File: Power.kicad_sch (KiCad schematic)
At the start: 14 parts, among them J2 S2B-PH-SM4-TB, Q1 DMP3099L, U2 AP2112K-3.3, U3 BQ21040DBV

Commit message: Added power latch circuit.
Signed-off-by: James Mendel <jrm.mendel@gmail.com>
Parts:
- added C7: 0.1u, symbol Device:C
- added D3, D4: MBR0520, Diode_SMD:D_SOD-123, symbol Diode:MBR0520
- added Q2: 2N7002, Package_TO_SOT_SMD:SOT-23, symbol Transistor_FET:2N7002
- added R10, R12, R13, R8, R9: 10k, symbol Device:R
- added SW1: CK_KMS2xxGP, Button_Switch_SMD:SW_SPST_CK_KMS2xxGP, symbol Switch:CK_KMS2xxGP
- D1: value CHARGE -> CHARGING
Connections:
- net +3.3V: now also D3.2 (A)
- net GND: now also C7.2, Q2.2 (S), R10.2, R13.1, R8.2, SW1.SH (B)
- net PWR_EN: now also Q2.3 (D), R12.2, R8.1
- net V_SW: now also SW1.1
- new net: D3.1 (K), D4.1 (K), R12.1
- new net: D4.2 (A), R9.2, SW1.2
- new net PWR_SW: C7.1, R10.1, R9.1
- new net SYS_PWROFF: Q2.1 (G), R13.2
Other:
- note added: "Off-Sheet Connections"
- note added: "Power Switch + Latch"
- note removed: "Todo: Power switching with tactile button."
- moved on the sheet: C3, C4, C5, C6, D1, D2, J2, Q1, R4, R5, R6, R7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

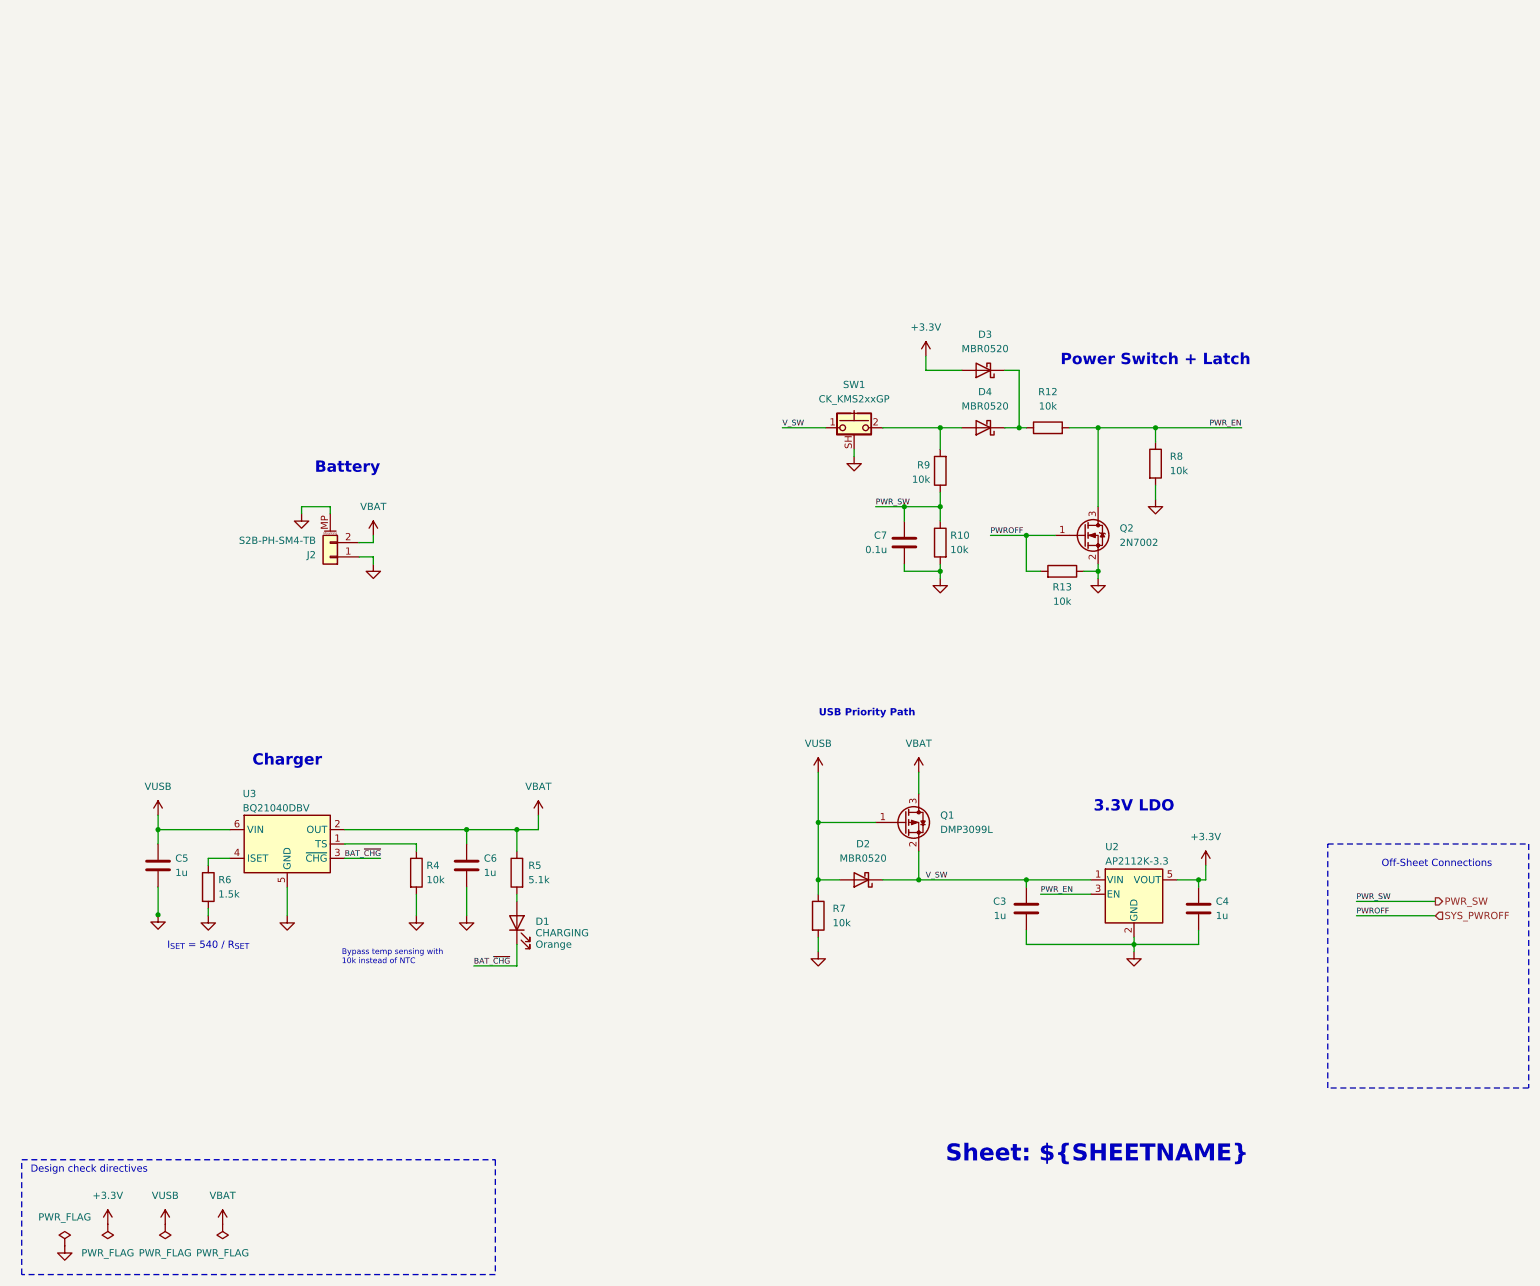
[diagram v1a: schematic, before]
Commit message: SCH and PCB updates. Added Integrated GPS and other features.
Signed-off-by: James Mendel <jrm.mendel@gmail.com>
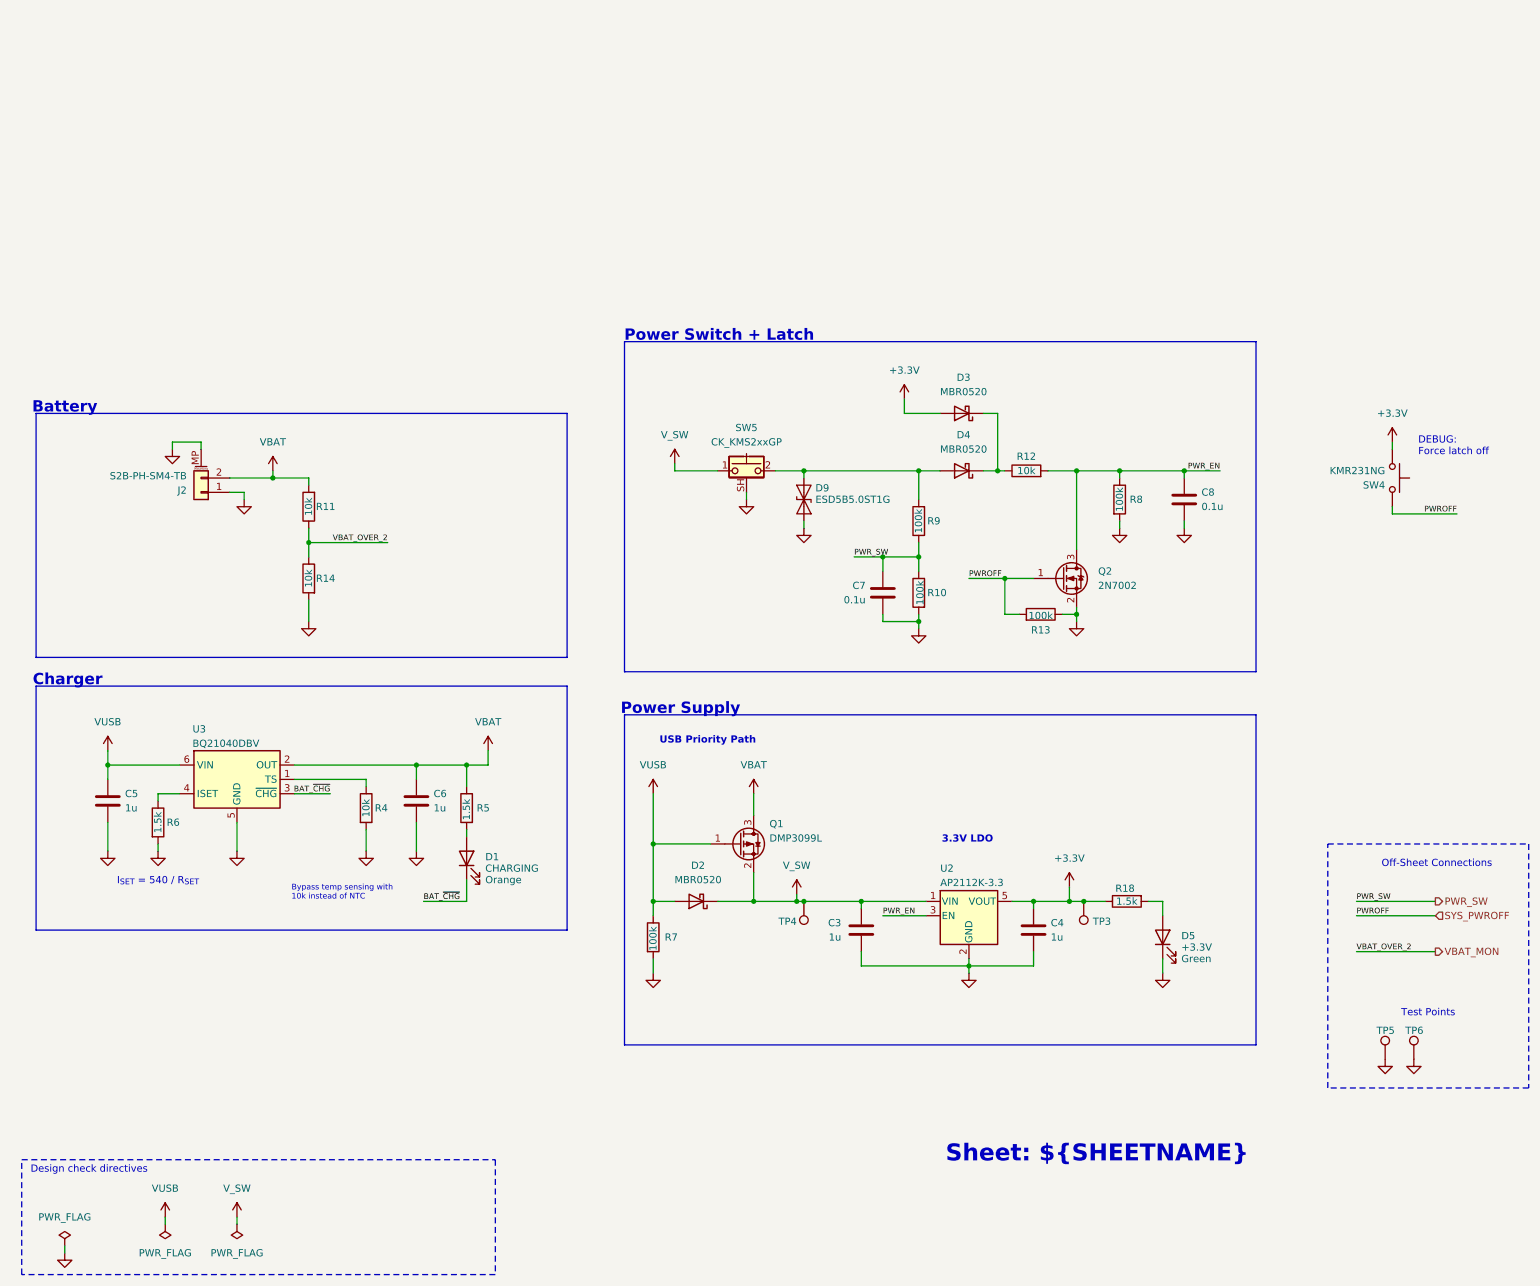
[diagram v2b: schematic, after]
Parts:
- removed SW1: CK_KMS2xxGP, Button_Switch_SMD:SW_SPST_CK_KMS2xxGP, symbol Switch:CK_KMS2xxGP
- added C8: 0.1u, Capacitor_SMD:C_0603_1608Metric, symbol Device:C
- added D5: +3.3V, Diode_SMD:D_0603_1608Metric, symbol Device:LED
- added D9: ESD5B5.0ST1G, Diode_SMD:D_SOD-523, symbol Diode:ESD9B5.0ST5G
- added R11, R14: 10k, Resistor_SMD:R_0603_1608Metric, symbol Device:R
- added R18: 1.5k, Resistor_SMD:R_0603_1608Metric, symbol Device:R
- added SW4: KMR231NG, Button_Switch_SMD:SW_Push_1P1T_NO_CK_KMR2, symbol Switch:SW_Push
- added SW5: CK_KMS2xxGP, Button_Switch_SMD:SW_SPST_CK_KMS2xxGP, symbol Switch:CK_KMS2xxGP
- added TP3, TP5, TP6: 3.3V, TestPoint:TestPoint_Pad_D1.5mm, symbol Connector:TestPoint
- added TP4: V_SW, TestPoint:TestPoint_Pad_D1.5mm, symbol Connector:TestPoint
- C3, C4, C5, C6, C7: footprint (none) -> Capacitor_SMD:C_0603_1608Metric
- D1: footprint (none) -> Diode_SMD:D_0603_1608Metric; MPN (none) -> LTST-C190KFKT
- R10, R13, R7, R8, R9: value 10k -> 100k; footprint (none) -> Resistor_SMD:R_0603_1608Metric
- R12, R4, R6: footprint (none) -> Resistor_SMD:R_0603_1608Metric
- R5: value 5.1k -> 1.5k; footprint (none) -> Resistor_SMD:R_0603_1608Metric
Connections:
- net +3.3V: now also R18.1, SW4.1, TP3.1
- net GND: now also C8.2, D5.1 (K), D9.1 (A1), R14.2, SW5.SH (B), TP5.1, TP6.1
- net PWR_EN: now also C8.1
- net SYS_PWROFF: now also SW4.2
- net VBAT: now also R11.2
- net V_SW: now also SW5.1, TP4.1
- net at D4.2 (A), R9.2: now also D9.2 (A2), SW5.2
- new net: D5.2 (A), R18.2
- new net VBAT_MON: R11.1, R14.1
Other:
- note added: "DEBUG: Force latch off"
- note added: "Power Supply"
- note added: "Test Points"
- moved on the sheet: C3, C4, C5, C6, C7, D1, D2, D3, D4, J2, Q1, Q2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

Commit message: Updated board outline to version 004
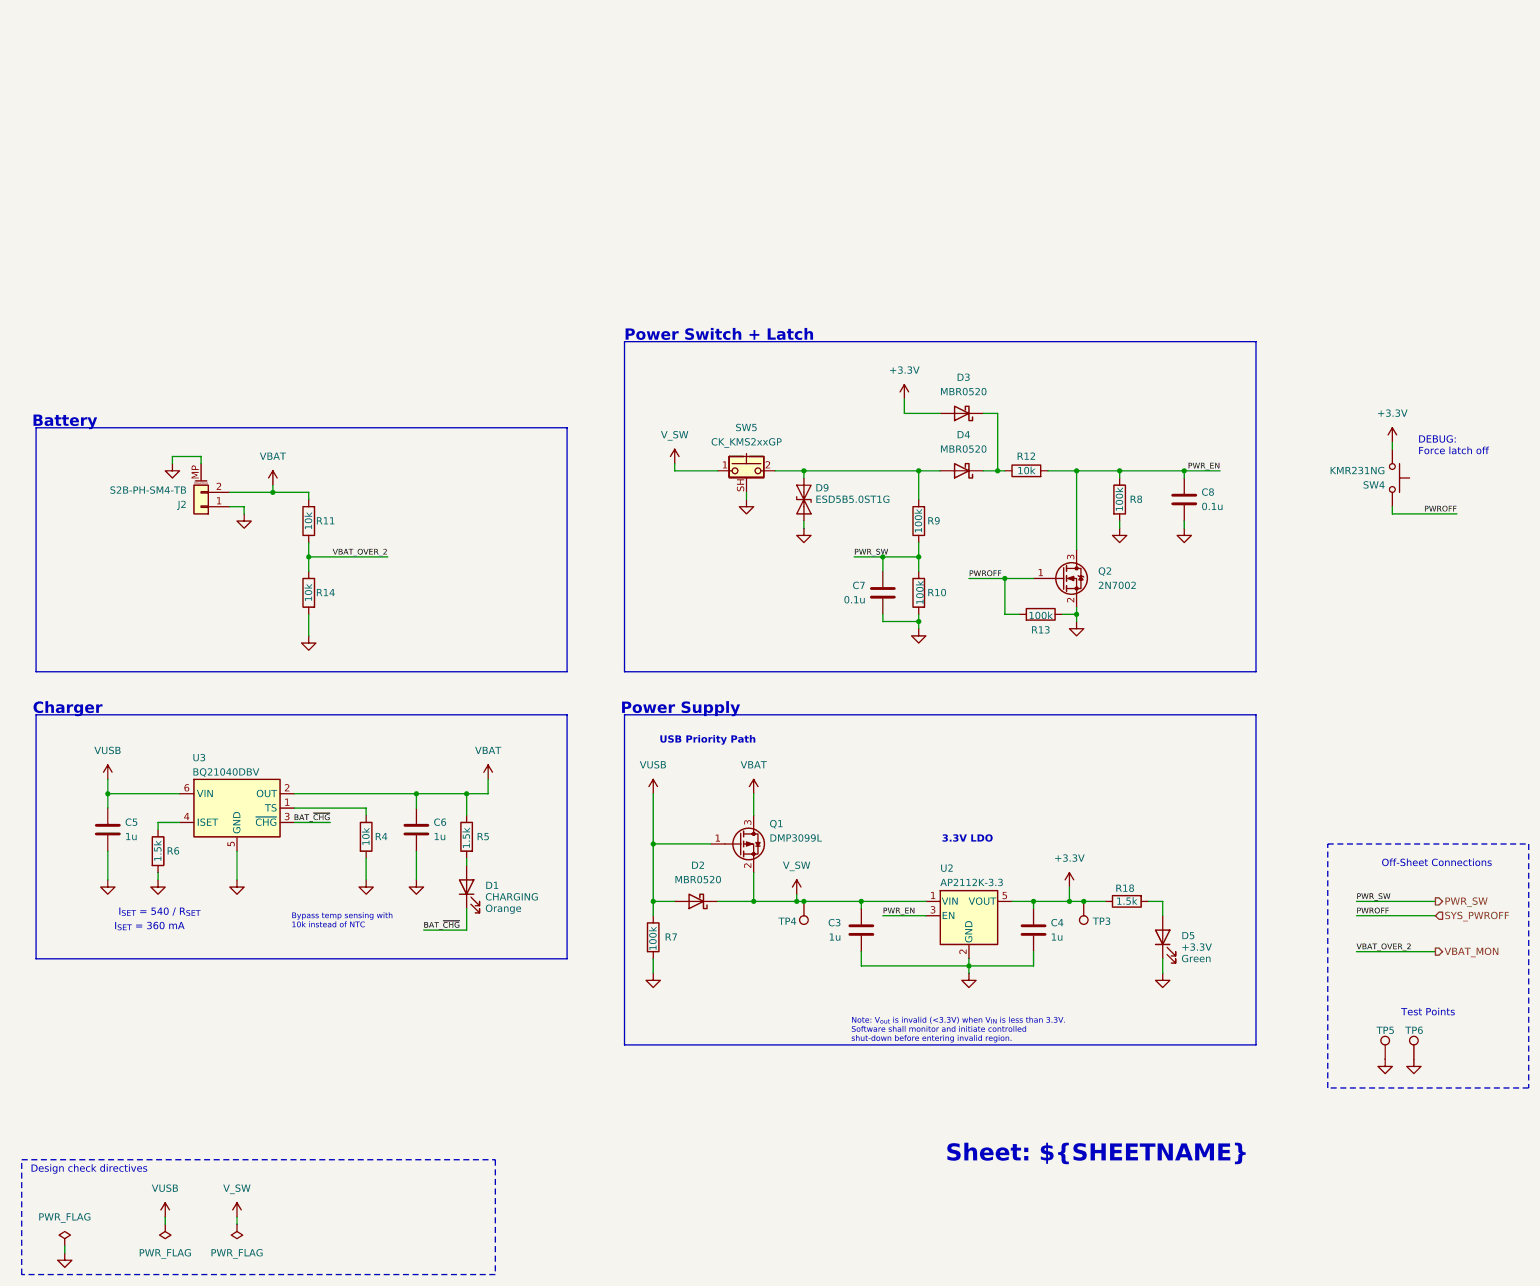
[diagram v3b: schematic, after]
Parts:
- TP3, TP4: footprint TestPoint:TestPoint_Pad_D1.5mm -> M20048-1:TestPoint_Pad_D1.5mm_WITH_LABEL
- TP5, TP6: value 3.3V -> GND; footprint TestPoint:TestPoint_Pad_D1.5mm -> M20048-1:TestPoint_Pad_D1.5mm_WITH_LABEL
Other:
- note added: "I_{SET} = 360 mA"
- note added: "Note: V_{out} is invalid (<3.3V) when V_{IN} is less than 3.3V. Software shall monitor and initiate controlled shut-down before entering invalid region."
- moved on the sheet: C5, C6, D1, J2, R11, R14, R4, R5, R6, U3

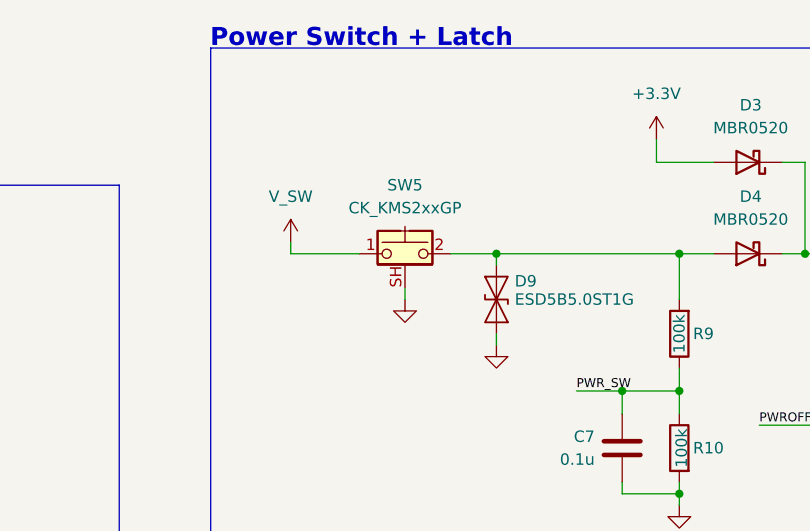
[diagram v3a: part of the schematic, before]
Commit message: Component placement for -004 board outline.
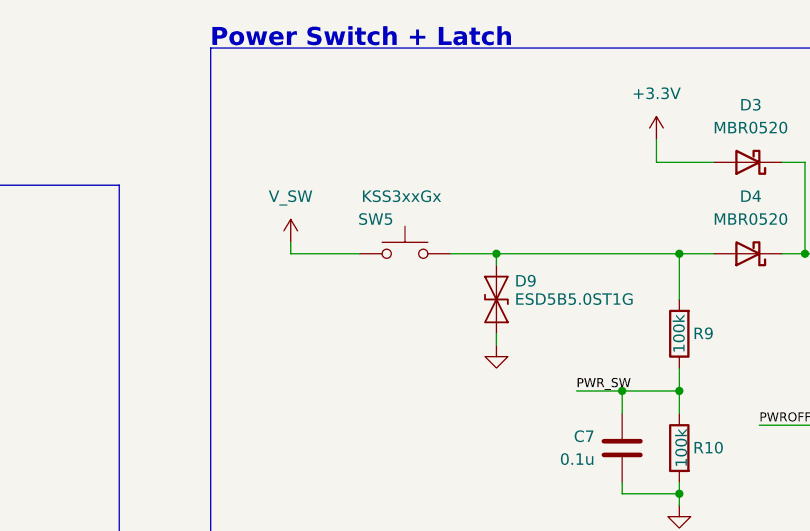
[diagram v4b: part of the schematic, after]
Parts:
- removed SW5: CK_KMS2xxGP, Button_Switch_SMD:SW_SPST_CK_KMS2xxGP, symbol Switch:CK_KMS2xxGP
- added SW5: KSS3xxGx, C&K:SW_KSS323_CNK, symbol Switch:SW_Push
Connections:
- net V_SW: now also SW5.1
- net at D4.2 (A), D9.2 (A2), R9.2: now also SW5.2
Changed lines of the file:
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@@
-		)
-	)
-	(wire
-		(pts
-			(xy 143.51 57.15) (xy 143.51 58.42)
-		)
-		(stroke
-			(width 0)
-			(type default)
 		)
 	)
@@
 	)
 	(symbol
-		(lib_id "Switch:CK_KMS2xxGP")
-		(at 143.51 53.34 0)
-		(unit 1)
-		(exclude_from_sim no)
-		(in_bom yes)
-		(on_board yes)
-		(dnp no)
-		(fields_autoplaced yes)
-		(property "Reference" "SW5"
-			(at 143.51 45.72 0)
-			(effects
-				(font
-					(size 1.27 1.27)
-				)
-			)
-		)
-		(property "Value" "CK_KMS2xxGP"
-			(at 143.51 48.26 0)
-			(effects
-				(font
-					(size 1.27 1.27)
-				)
-			)
-		)
-		(property "Footprint" "Button_Switch_SMD:SW_SPST_CK_KMS2xxGP"
-			(at 143.51 48.26 0)
-			(effects
-				(font
-					(size 1.27 1.27)
-				)
-				(hide yes)
-			)
-		)
-		(property "Datasheet" "https://www.ckswitches.com/media/1482/kms.pdf"
-			(at 143.51 48.26 0)
-			(effects
-				(font
-					(size 1.27 1.27)
-				)
-				(hide yes)
-			)
-		)
-		(property "Description" "Microminiature SMT Side Actuated, 4.2 x 2.8 x 1.42mm, with pegs, with shield pin"
-			(at 143.51 53.34 0)
-			(effects
-				(font
-					(size 1.27 1.27)
-				)
-				(hide yes)
-			)
-		)
-		(pin "SH"
-		)
-		(pin "1"
-		)
-		(pin "2"
-		)
-		(instances
-			(project "Terra-HW"
-				(path "/acca4a2f-1cc7-44b0-a26a-921257f6c268/5f0d062d-9fa8-4c48-be05-0b92e4e6324b"
-					(reference "SW5")
-					(unit 1)
-				)
-			)
-		)
-	)
-	(symbol
 		(lib_id "Device:R")
 		(at 210.82 129.54 90)
@@
 	(symbol
 		(lib_id "power:GND")
-		(at 143.51 58.42 0)
-		(unit 1)
-		(exclude_from_sim no)
-		(in_bom yes)
-		(on_board yes)
-		(dnp no)
-		(fields_autoplaced yes)
-		(property "Reference" "#PWR064"
-			(at 143.51 64.77 0)
-			(effects
-				(font
-					(size 1.27 1.27)
-				)
-				(hide yes)
-			)
-		)
-		(property "Value" "GND"
-			(at 143.51 63.5 0)
-			(effects
-				(font
-					(size 1.27 1.27)
-				)
-				(hide yes)
-			)
-		)
-		(property "Footprint" ""
-			(at 143.51 58.42 0)
-			(effects
-				(font
-					(size 1.27 1.27)
-				)
-				(hide yes)
-			)
-		)
-		(property "Datasheet" ""
-			(at 143.51 58.42 0)
-			(effects
-				(font
-					(size 1.27 1.27)
-				)
-				(hide yes)
-			)
-		)
-		(property "Description" "Power symbol creates a global label with name \"GND\" , ground"
-			(at 143.51 58.42 0)
-			(effects
-				(font
-					(size 1.27 1.27)
-				)
-				(hide yes)
-			)
-		)
-		(pin "1"
-		)
-		(instances
-			(project "Terra-HW"
-				(path "/acca4a2f-1cc7-44b0-a26a-921257f6c268/5f0d062d-9fa8-4c48-be05-0b92e4e6324b"
-					(reference "#PWR064")
-					(unit 1)
-				)
-			)
-		)
-	)
-	(symbol
-		(lib_id "power:GND")
 		(at 127 142.24 0)
 		(unit 1)
@@
 					(unit 1)
 				)
+			)
+		)
+	)
+	(symbol
+		(lib_id "Switch:SW_Push")
+		(at 143.51 53.34 0)
+		(unit 1)
+		(exclude_from_sim no)
+		(in_bom yes)
+		(on_board yes)
+		(dnp no)
+		(property "Reference" "SW5"
+			(at 142.24 49.53 0)
+			(effects
+				(font
+					(size 1.27 1.27)
+				)
+				(justify right)
+			)
+		)
+		(property "Value" "KSS3xxGx"
+			(at 147.574 46.99 0)
+			(effects
+				(font
+					(size 1.27 1.27)
+				)
+				(justify right)
+			)
+		)
+		(property "Footprint" "C&K:SW_KSS323_CNK"
+			(at 143.51 48.26 0)
+			(effects
+				(font
+					(size 1.27 1.27)
+				)
+				(hide yes)
+			)
+		)
+		(property "Datasheet" "https://www.ckswitches.com/media/1463/kss.pdf"
+			(at 143.51 48.26 0)
+			(effects
+				(font
+					(size 1.27 1.27)
+				)
+				(hide yes)
+			)
+		)
+		(property "Description" "Tactile Switch SPST-NO Side Actuated Surface Mount, Right Angle"
+			(at 143.51 53.34 0)
+			(effects
+				(font
+					(size 1.27 1.27)
+				)
+				(hide yes)
+			)
+		)
+		(property "MPN" "KSS323GLFG"
+			(at 143.51 53.34 0)
+			(effects
+				(font
+					(size 1.27 1.27)
+				)
+				(hide yes)
+			)
+		)
+		(pin "2"
+		)
+		(pin "1"
+		)
+		(instances
+			(project "Terra-HW"
+				(path "/acca4a2f-1cc7-44b0-a26a-921257f6c268/5f0d062d-9fa8-4c48-be05-0b92e4e6324b"
+					(reference "SW5")
+					(unit 1)
+				)

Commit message: Lots of board layout
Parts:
- added C17, C18: 0.1u, Capacitor_SMD:C_0603_1608Metric, symbol Device:C
- added D11: MBR0520, Diode_SMD:D_SOD-123, symbol Diode:MBR0520
- added Q3: 2N7002, Package_TO_SOT_SMD:SOT-23, symbol Transistor_FET:2N7002
- added R17: 10k, Resistor_SMD:R_0603_1608Metric, symbol Device:R
- added R27, R28, R29: 100k, Resistor_SMD:R_0603_1608Metric, symbol Device:R
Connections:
- net GND: now also C17.2, C18.2, Q3.2 (S), R29.2
- net VBAT_MON: now also C18.1
- net at D3.1 (K), D4.1 (K), R12.1: now also D11.1 (K)
- new net: R28.2, R29.1
- new net: C17.1, Q3.1 (G), R27.2, R28.1
- new net: D11.2 (A), Q3.3 (D), R17.1
- new net V_USB: R17.2, R27.1
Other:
- note added: "Force power off"
- note added: "Layout Note: Place cap near ADC"
- note removed: "DEBUG: Force latch off"
- moved on the sheet: R12, SW4

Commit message: More layout and sch updates, ready for final review.
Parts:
- D11, D2, D3, D4: value MBR0520 -> PMEG2010AEH; MPN (none) -> PMEG2010AEH
- D9: value ESD5B5.0ST1G -> DESD5V0U1BB-7; MPN (none) -> DESD5V0U1BB-7
- J2: MPN (none) -> S2B-PH-SM4-TB
- Q1: MPN (none) -> DMP3099L
- Q2, Q3: MPN (none) -> 2N7002
- SW4: MPN (none) -> KMR231NG
- U3: MPN (none) -> BQ21040DBV
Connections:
- net V_USB is gone; now on net VUSB: R17.2, R27.1
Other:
- note added: "3V3 Latch"
- note added: "Button Press"
- note added: "Power Switch"
- note added: "USB"
- note added: "USB Detect"
- note added: "or"
- moved on the sheet: C17, C18, C3, C4, C5, C6, C7, C8, D1, D11, D2, D3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
